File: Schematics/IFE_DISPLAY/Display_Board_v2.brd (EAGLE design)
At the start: 108 x 83.8 mm, 79 parts, among them Q1 16MHz, Q3 16MHz, U4 HEX_CONVERTER, U5 HEX_CONVERTER

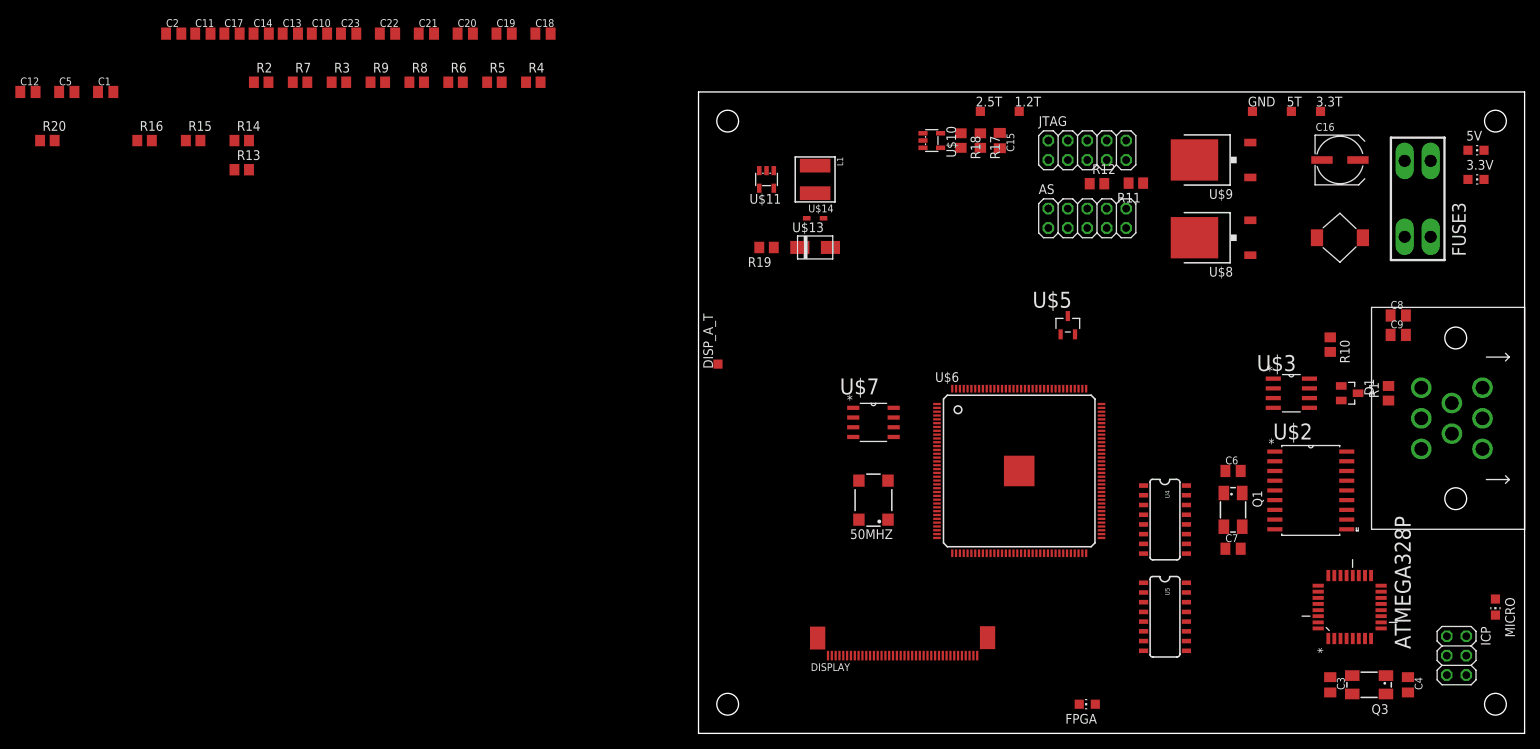
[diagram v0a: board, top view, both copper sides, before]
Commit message: Need to fix oscillators, Initial placement done
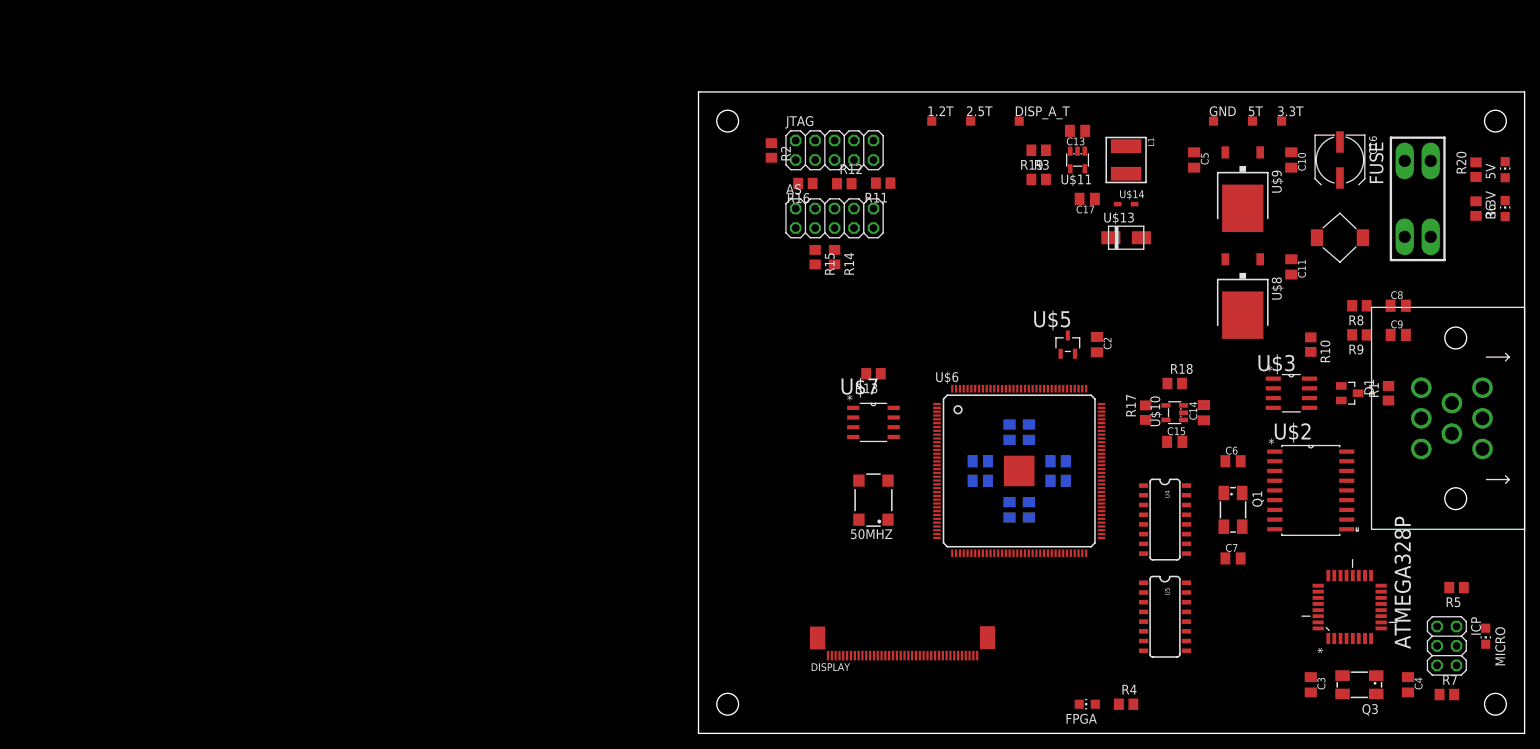
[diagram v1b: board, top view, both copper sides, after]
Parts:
- moved R20 186.7 mm to (101.6, 73.7), turned to 90 degrees
- moved R7 169.9 mm to (97.8, 5.08)
- moved C5 147.6 mm to (64.8, 74.9), turned to 270 degrees
- moved C11 145.5 mm to (77.5, 61.0), turned to 270 degrees
- moved R5 142.0 mm to (99.1, 19.1), turned to 180 degrees
- moved C12 135.8 mm to (40.6, 39.4), flipped to the bottom, turned to 270 degrees
- moved R6 134.4 mm to (101.6, 68.6), turned to 270 degrees
- moved C14 132.8 mm to (66.0, 41.9), turned to 90 degrees
- moved R9 132.5 mm to (86.4, 52.1), turned to 180 degrees
- moved C1 128.6 mm to (43.2, 39.4), flipped to the bottom, turned to 270 degrees
- moved C10 128.1 mm to (77.5, 74.9), turned to 270 degrees
- moved C2 127.3 mm to (52.1, 50.8), turned to 270 degrees
- moved R8 126.6 mm to (86.4, 55.9), turned to 180 degrees
- moved C17 113.8 mm to (50.8, 69.8), turned to 180 degrees
- moved R4 112.3 mm to (55.9, 3.81)
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- renumbered FUSE3 to FUSE
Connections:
- removed net IO100: U$6.100
- removed net N$11: U$6.109, U$6.37
- removed net N$9: U$6.107, U$6.35
- net FPGA_D0_3_3: now also U$6.87
- net FPGA_D1_3_3: now also U$6.86
- net FPGA_D2_3_3: now also U$6.85
- net FPGA_D3_3_3: now also U$6.100
- net FPGA_R0_3_3: now also U$6.77, U5.10; no longer U5.2
- net FPGA_R1_3_3: now also U$6.80, U5.6; no longer U5.4
- net FPGA_R2_3_3: now also U$6.83, U5.4; no longer U5.6
- net FPGA_R3_3_3: now also U$6.84, U5.2; no longer U5.10
- net FPGA_REG0: now also U5.9; no longer U5.3
- net FPGA_REG1: now also U5.7; no longer U5.5
- net FPGA_REG2: now also U5.5; no longer U5.7
- net FPGA_REG3: now also U5.3; no longer U5.9
- net FPGA_RSEL_3_3: now also U$6.105
- net FPGA_W_3_3: now also U$6.106
- net V+: now also U$6.107, U$6.35
- net VCC: now also U$6.109, U$6.37

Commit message: Updted Oscillators, routing ~60%
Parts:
- removed 50MHZ: SM77H, crystal:SM77H
- removed Q1, Q3: 16MHz, adafruit:CTS406
- added U$1: SM77H, Display_Custom:SM77H
- added U$15: 406CYRYSTAL, Display_Custom:CTS406
- added U$4: 16MHz, Display_Custom:CTS406
- turned R1 to 270 degrees
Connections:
- net +3V3: now also U$1.4; no longer 50MHZ.4
- net 2515_OSC1: now also U$15.3; no longer Q1.3
- net 2515_OSC2: now also U$15.1; no longer Q1.1
- net 50_MHZ: now also U$1.3; no longer 50MHZ.3
- net GND: now also U$1.2; no longer 50MHZ.2
- net XTAL1: now also U$4.3; no longer Q3.3
- net XTAL2: now also U$4.1; no longer Q3.1
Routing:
- net +5V: track 0.00 -> 100.8 mm
- net DISP_PWM: track 0.00 -> 79.9 mm, vias 0 -> 4
- net +3V3: track 0.00 -> 57.0 mm
- net LED1: track 0.00 -> 57.0 mm, vias 0 -> 2
- net NCONFIG: track 0.00 -> 40.1 mm
- net CANL: track 0.00 -> 36.3 mm
- net FPGA_REG1: track 0.00 -> 33.4 mm, vias 0 -> 2
- net FPGA_REG3: track 0.00 -> 31.8 mm, vias 0 -> 2
- net FPGA_REG2: track 0.00 -> 31.5 mm, vias 0 -> 2
- net MOSI: track 0.00 -> 30.4 mm, vias 0 -> 2
- net +12V: track 0.00 -> 29.5 mm
- net FPGA_DATA2: track 0.00 -> 28.5 mm, vias 0 -> 2
- net DISP_LEDA: track 0.00 -> 26.7 mm
- net PWR_IN_12: track 0.00 -> 25.9 mm
- net MISO: track 0.00 -> 25.8 mm
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
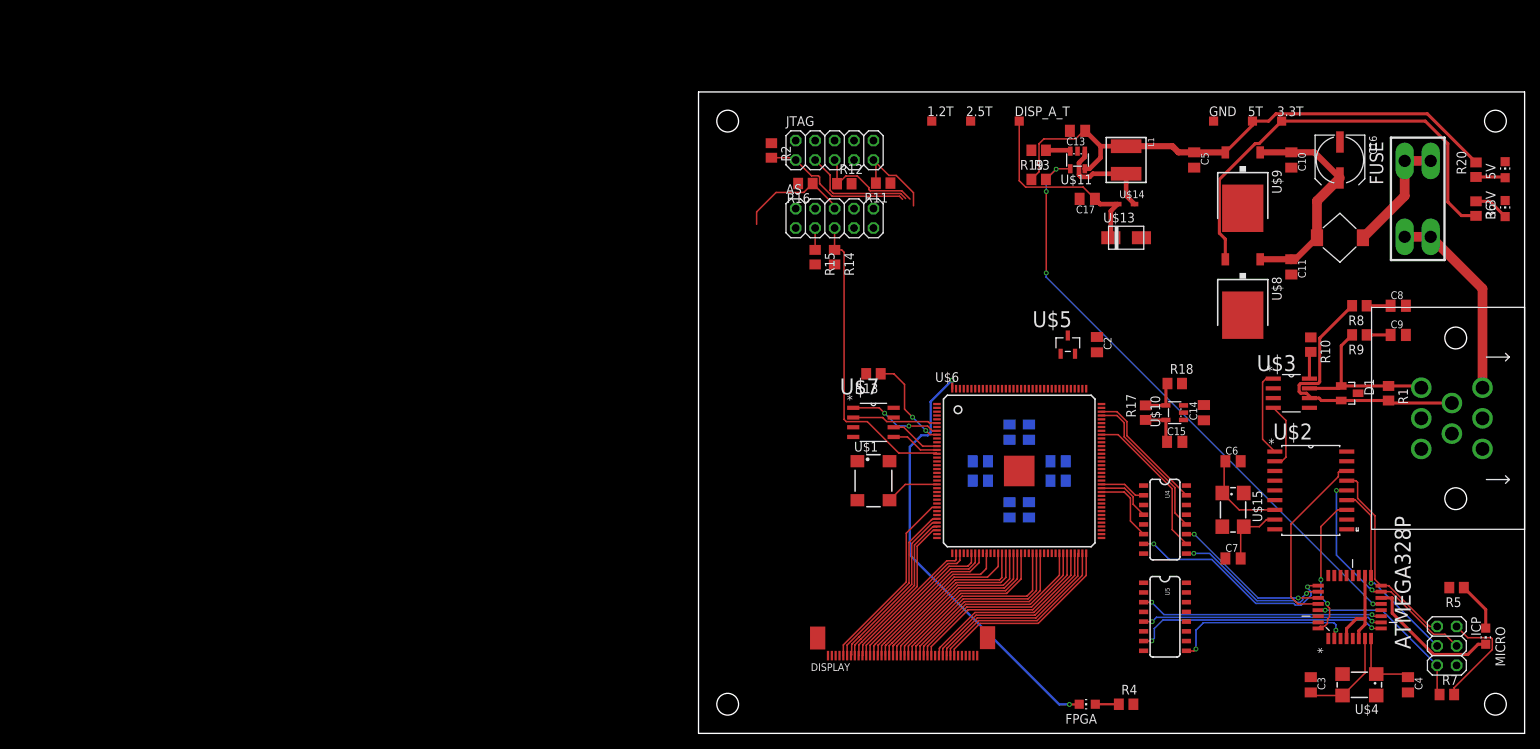
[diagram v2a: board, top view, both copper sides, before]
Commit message: Finished Routing, Adding LOGO
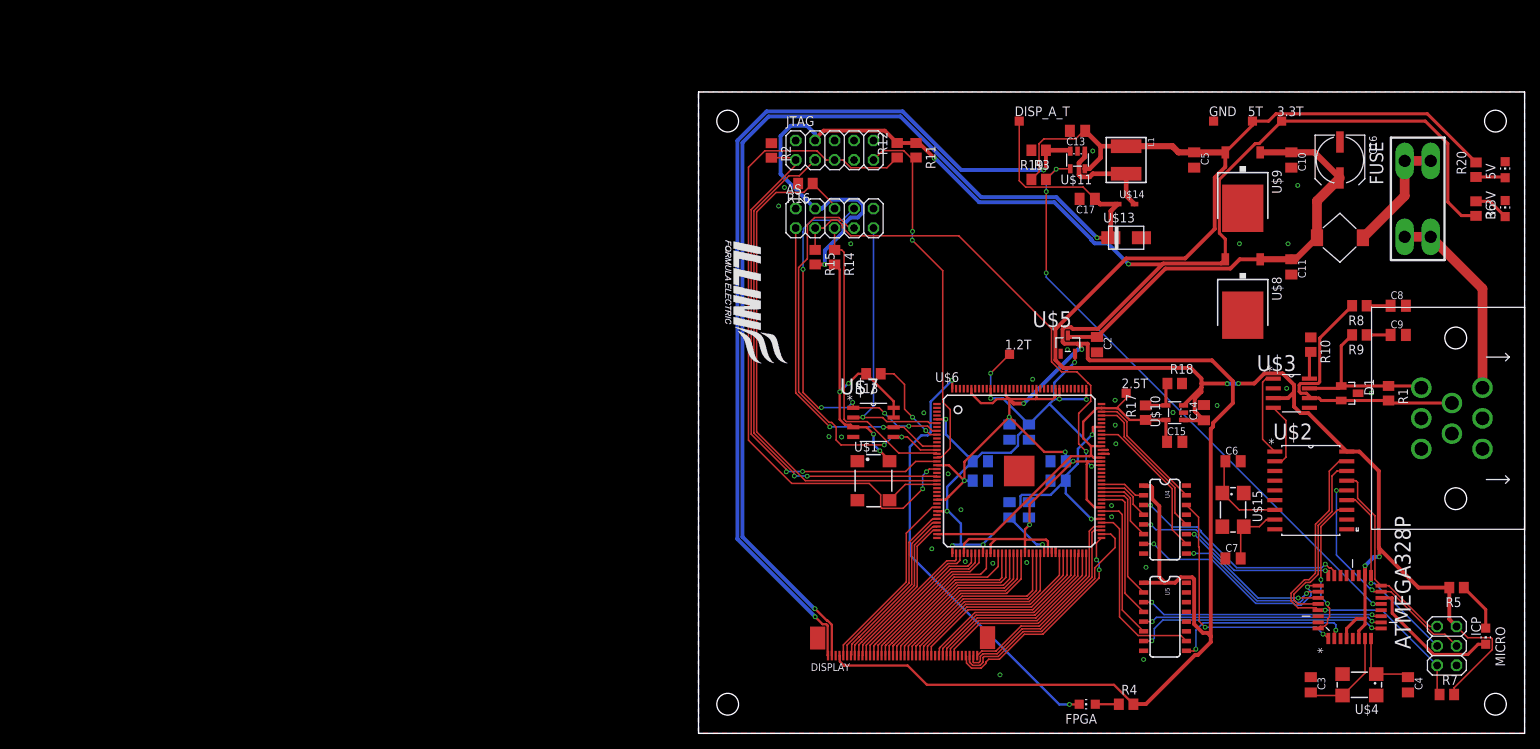
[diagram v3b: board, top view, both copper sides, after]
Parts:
- moved 2.5T 41.0 mm to (55.9, 44.5)
- moved 1.2T 32.1 mm to (40.6, 49.5)
- moved R12 8.17 mm to (26.0, 76.2), turned to 90 degrees
- moved R11 6.07 mm to (28.4, 76.2), turned to 270 degrees
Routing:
- net +3V3: track 57.0 -> 471.5 mm, vias 0 -> 14
- net +5V: track 100.8 -> 239.4 mm, vias 0 -> 4
- net DISP_LEDA: track 26.7 -> 154.8 mm, vias 0 -> 2
- net DISP_LEDK: track 3.23 -> 123.2 mm, vias 0 -> 2
- net VCC: track 0.00 -> 118.3 mm, vias 0 -> 12
- net TMS: track 14.6 -> 89.8 mm, vias 0 -> 2
- net CONF_DONE: track 2.86 -> 64.2 mm, vias 0 -> 2
- net NCE: track 14.9 -> 68.3 mm
- net TDO: track 15.1 -> 66.3 mm, vias 0 -> 2
- net TCK: track 19.9 -> 68.6 mm, vias 0 -> 2
- net DATA0: track 6.36 -> 53.5 mm, vias 0 -> 2
- net V+: track 5.58 -> 49.7 mm
- net NCSO: track 12.2 -> 49.7 mm, vias 2 -> 5
- net TDI: track 11.9 -> 48.9 mm, vias 0 -> 2
- net DCLK: track 6.68 -> 42.9 mm, vias 0 -> 2
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- added copper zone on layer 1, net GND
- added copper zone on layer 16, net GND
